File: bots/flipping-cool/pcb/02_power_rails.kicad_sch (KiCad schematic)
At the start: 6 parts, among them J5 POLOLU_D36V50F6_6V_5P5A_BEC

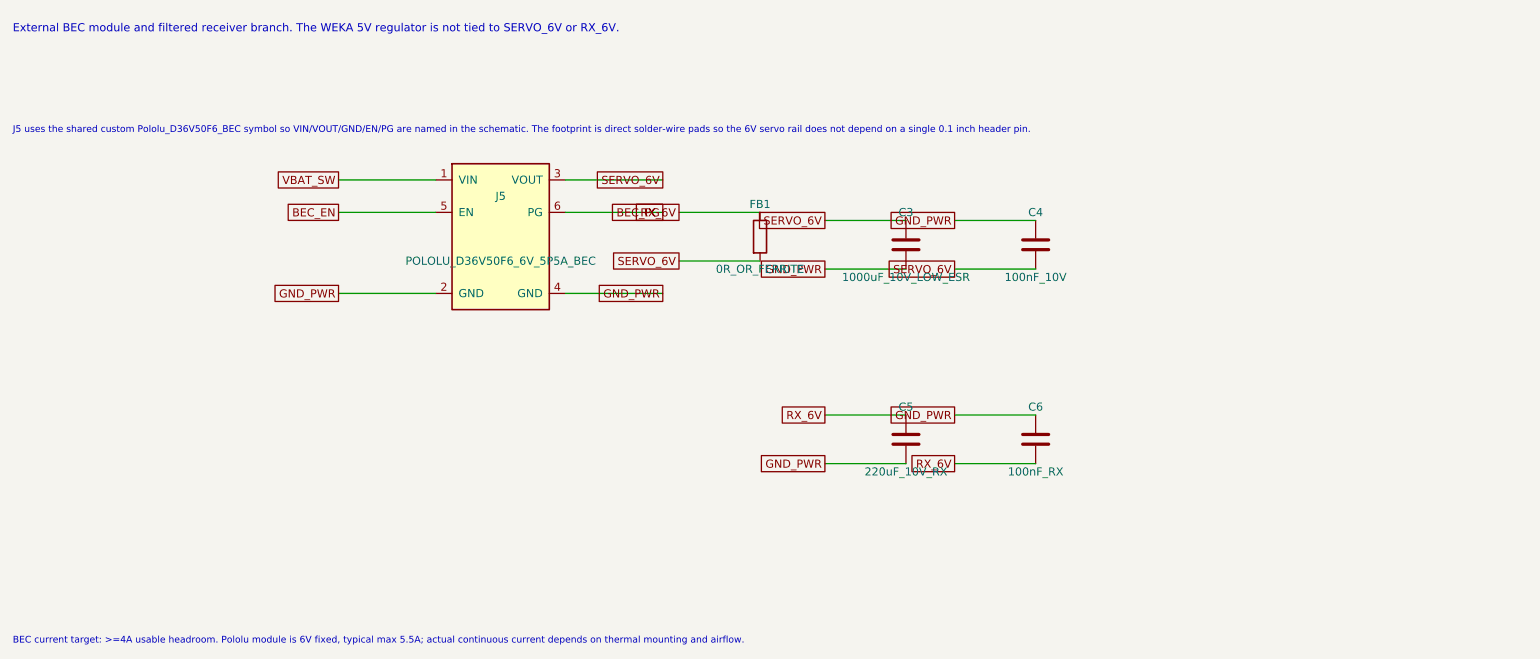
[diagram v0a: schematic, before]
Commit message: Refactor Flipping Cool PCB design to Rev B, updating title, date, and revision details. Integrate ESP32-S3 module and enhance documentation for MCU I/O and debugging features, while maintaining historical context from Rev A.
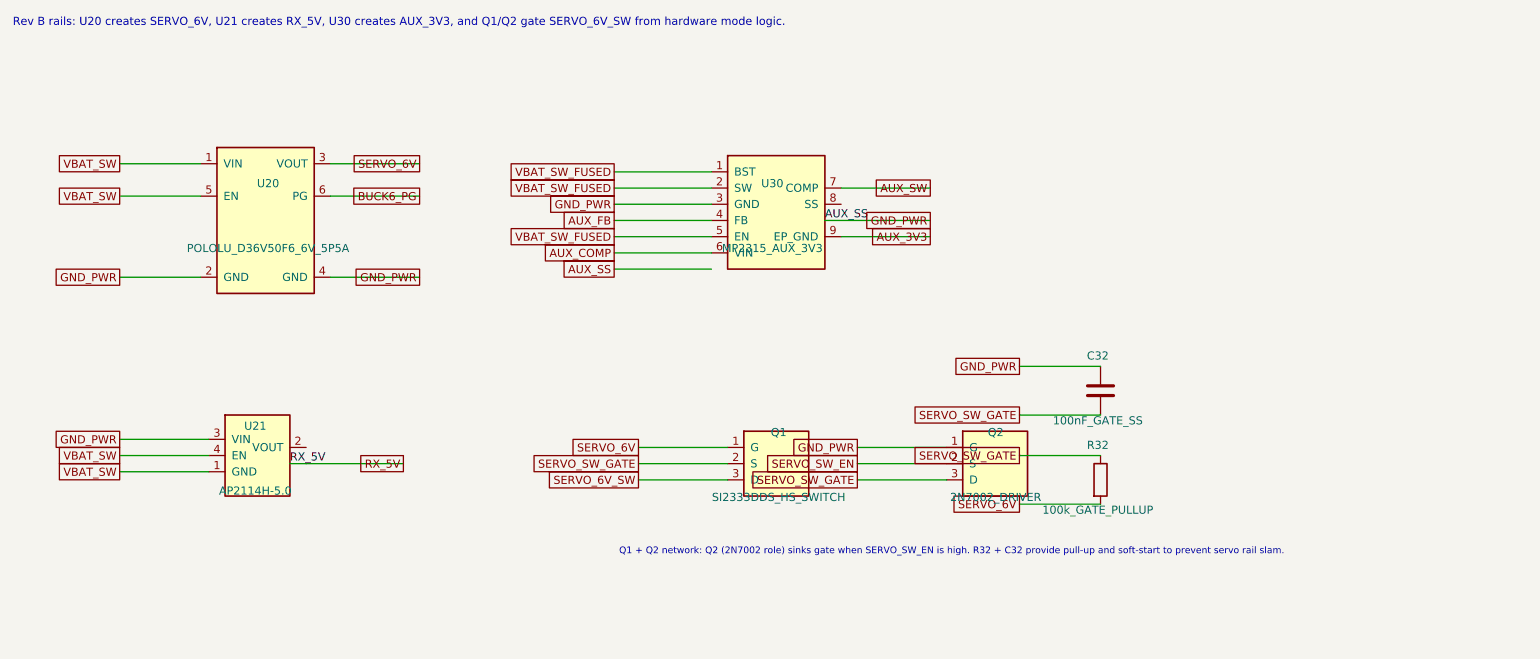
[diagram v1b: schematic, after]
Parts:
- removed C3: 1000uF_10V_LOW_ESR, Capacitor_THT:CP_Radial_D8.0mm_P3.50mm, symbol Device:C
- removed C4: 100nF_10V, Capacitor_SMD:C_0805_2012Metric, symbol Device:C
- removed C5: 220uF_10V_RX, Capacitor_THT:CP_Radial_D6.3mm_P2.50mm, symbol Device:C
- removed C6: 100nF_RX, Capacitor_SMD:C_0805_2012Metric, symbol Device:C
- removed FB1: 0R_OR_FERRITE, Resistor_SMD:R_1206_3216Metric, symbol Device:R
- added C32: 100nF_GATE_SS, Capacitor_SMD:C_0805_2012Metric, symbol Device:C
- added Q1: SI2333DDS_HS_SWITCH, Package_TO_SOT_SMD:SOT-23, symbol custom:PMOS_SI2333DDS
- added Q2: 2N7002_DRIVER, Package_TO_SOT_SMD:SOT-23, symbol custom:PMOS_SI2333DDS
- added R32: 100k_GATE_PULLUP, Resistor_SMD:R_0805_2012Metric, symbol Device:R
- added U21: AP2114H-5.0, Package_TO_SOT_SMD:SOT-223-3_TabPin2, symbol custom:REG_AP2114H_5V
- added U30: MP2315_AUX_3V3, Package_SO:SOIC-8-1EP_3.9x4.9mm_P1.27mm_EP2.41x3.3mm, symbol custom:REG_MP2315_BUCK
- U20: renamed from J5; value POLOLU_D36V50F6_6V_5P5A_BEC -> POLOLU_D36V50F6_6V_5P5A; footprint Connector_Wire:SolderWire-0.75sqmm_1x06_P4.8mm_D1.25mm_OD2.3mm_Relief2x -> Connector_PinHeader_2.54mm:PinHeader_1x06_P2.54mm_Vertical
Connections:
- net BEC_EN is gone; now on net VBAT_SW: U20.5 (EN)
- net SERVO_6V: now also Q1.1 (G), R32.2
- net VBAT_SW: now also U21.1 (GND), U21.4 (EN)
- net BEC_PG renamed BUCK6_PG
- net GND_PWR renamed AUX_SS
- net AUX_SS: now also C32.1, Q2.1 (G), U21.3 (VIN), U30.3 (GND)
- new net AUX_3V3: U30.9 (EP_GND)
- new net AUX_COMP: U30.6 (VIN)
- new net AUX_FB: U30.4 (FB)
- new net AUX_SW: U30.7 (COMP)
- new net SERVO_6V_SW: Q1.3 (D)
- new net SERVO_SW_EN: Q2.2 (S)
- new net SERVO_SW_GATE: C32.2, Q1.2 (S), Q2.3 (D), R32.1
- new net VBAT_SW_FUSED: U30.1 (BST), U30.2 (SW), U30.5 (EN)
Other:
- note added: "Q1 + Q2 network: Q2 (2N7002 role) sinks gate when SERVO_SW_EN is high. R32 + C32 provide pull-up and soft-start to prevent servo rail slam."
- note added: "Rev B rails: U20 creates SERVO_6V, U21 creates RX_5V, U30 creates AUX_3V3, and Q1/Q2 gate SERVO_6V_SW from hardware mode logic."
- note removed: "BEC current target: >=4A usable headroom. Pololu module is 6V fixed, typical max 5.5A; actual continuous current depends on thermal mounting and airflow."
- note removed: "External BEC module and filtered receiver branch. The WEKA 5V regulator is not tied to SERVO_6V or RX_6V."
- note removed: "J5 uses the shared custom Pololu_D36V50F6_BEC symbol so VIN/VOUT/GND/EN/PG are named in the schematic. The footprint is direct solder-wire pads so the 6V servo rail does not depend on a single 0.1 inch header pin."
- title: Flipping Cool Rev A - Power Rails -> Flipping Cool Rev B - Power Rails
- moved on the sheet: U20

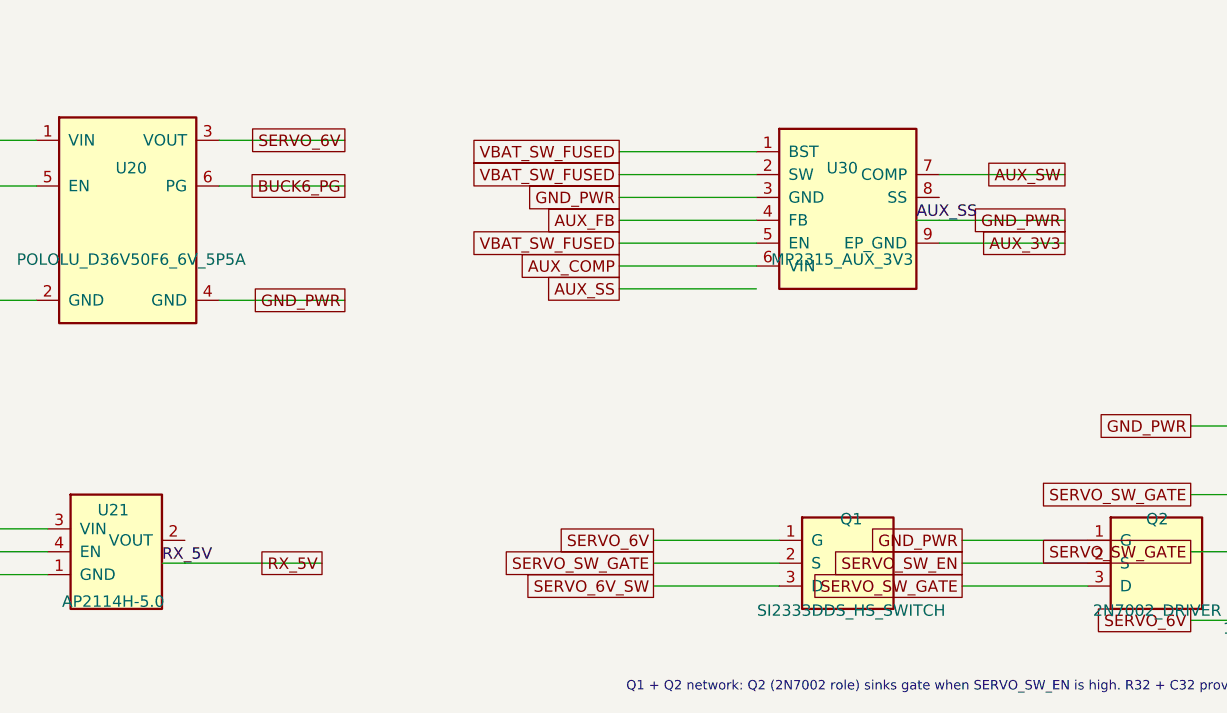
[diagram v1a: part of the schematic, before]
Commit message: Remove obsolete Flipping Cool Rev B project plan file and update schematic files to reflect the latest design changes, including integration of the ESP32-S3 module and enhancements to power management and control authority. Ensure all documentation is aligned with the current PCB design and architecture.
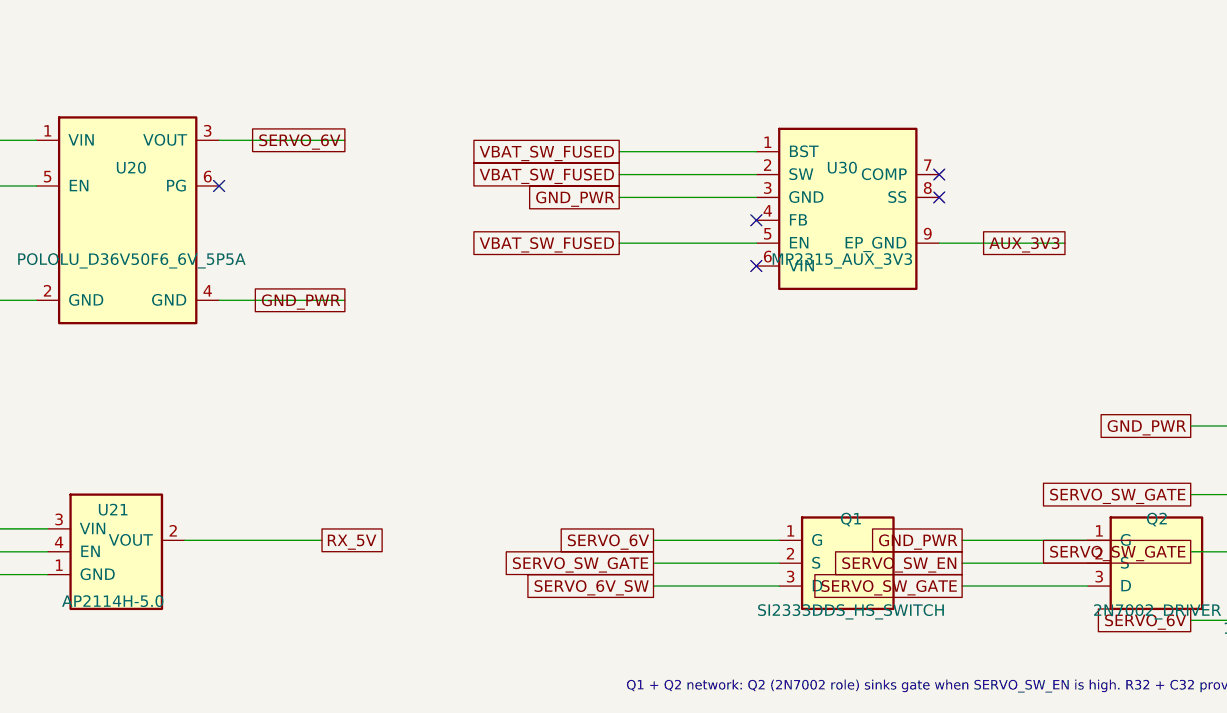
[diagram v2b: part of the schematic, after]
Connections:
- net RX_5V: now also U21.2 (VOUT)
- net AUX_COMP: no longer names the net of U30.6 (VIN)
- net AUX_FB: no longer names the net of U30.4 (FB)
- net AUX_SS renamed GND_PWR
- net AUX_SW: no longer names the net of U30.7 (COMP)
- net BUCK6_PG: no longer names the net of U20.6 (PG)
- no-connect marks 0 -> 5
